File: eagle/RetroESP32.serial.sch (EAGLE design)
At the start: 70 parts, among them J1 AUDIO_JACK_3.5MM_KIT, J2 SPKR, J3 Batt Conn, J5 503182-1852_503182-1852, J6 USB4110-GF-A_REVB, Q3 DMG3415U-7, Q4 mmbt2222, Q5 mmbt2222, U1 ESP32-WROVER, U3 XC6210B332MR-G, U4 MCP73832T-2ACI/OT, U6 LM4875

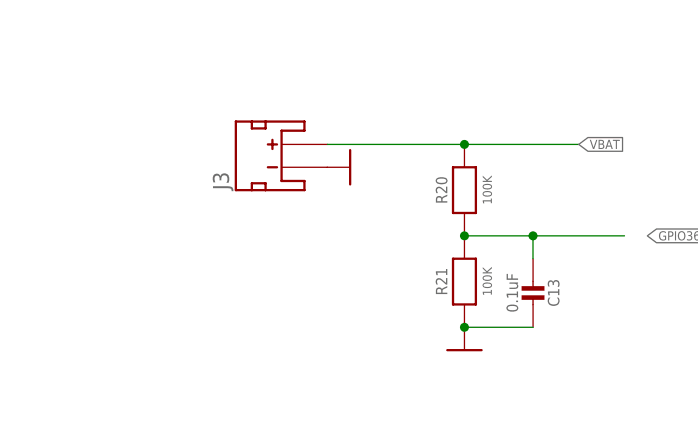
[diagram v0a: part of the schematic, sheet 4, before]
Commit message: feat: replaced JST with molex connector
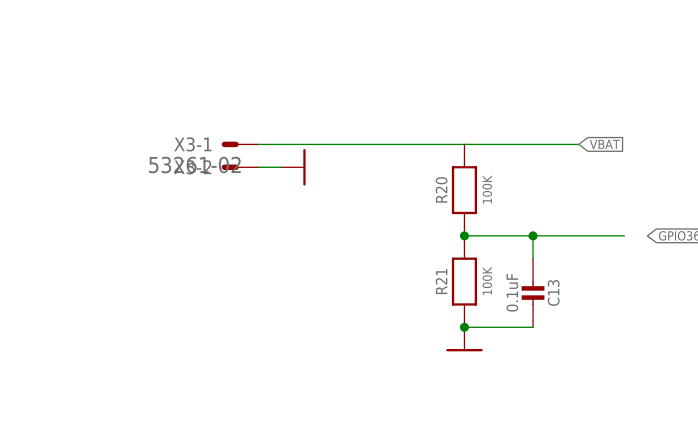
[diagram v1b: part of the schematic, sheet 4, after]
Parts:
- removed J2: SPKR, RetroESP32:CONN_02
- removed J3: Batt Conn, RetroESP32:JST_2MM_MALE
- added X2, X3: 53261-02, con-molex:53261-02
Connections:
- net GND: now also X3-2.S; no longer J3.-
- net VBAT: now also X3-1.S; no longer J3.+
- net VOUT1: now also X2-1.S; no longer J2.1
- net VOUT2: now also X2-2.S; no longer J2.2
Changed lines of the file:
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@@
 <layer number="56" name="wert" color="7" fill="1" visible="no" active="no"/>
 <layer number="57" name="tCAD" color="7" fill="1" visible="no" active="no"/>
+<layer number="58" name="b3D" color="7" fill="1" visible="no" active="no"/>
 <layer number="59" name="tCarbon" color="7" fill="1" visible="no" active="no"/>
 <layer number="60" name="bCarbon" color="7" fill="1" visible="no" active="no"/>
@@
 <layer number="154" name="FabDoc2" color="2" fill="1" visible="no" active="no"/>
 <layer number="155" name="FabDoc3" color="7" fill="15" visible="no" active="no"/>
+<layer number="156" name="DXF0409-TOP" color="7" fill="1" visible="no" active="no"/>
+<layer number="157" name="DXF0409-BOTTOM" color="7" fill="1" visible="no" active="no"/>
+<layer number="158" name="FaceMMeas" color="7" fill="1" visible="no" active="no"/>
+<layer number="159" name="Geh-Bear2" color="7" fill="1" visible="no" active="no"/>
+<layer number="160" name="Topologie" color="7" fill="1" visible="no" active="no"/>
+<layer number="161" name="tomplace2" color="7" fill="1" visible="no" active="no"/>
 <layer number="166" name="AntennaArea" color="7" fill="1" visible="yes" active="yes"/>
 <layer number="168" name="4mmHeightArea" color="7" fill="1" visible="yes" active="yes"/>
+<layer number="188" name="Graphics" color="15" fill="1" visible="yes" active="yes"/>
 <layer number="191" name="mNets" color="7" fill="1" visible="yes" active="yes"/>
 <layer number="192" name="mBusses" color="7" fill="1" visible="yes" active="yes"/>
@@
 <layer number="250" name="Descript" color="3" fill="1" visible="no" active="no"/>
 <layer number="251" name="SMDround" color="12" fill="11" visible="no" active="no"/>
+<layer number="252" name="BR-BS" color="7" fill="1" visible="no" active="no"/>
+<layer number="253" name="Extra" color="7" fill="1" visible="no" active="no"/>
 <layer number="254" name="cooling" color="7" fill="1" visible="yes" active="yes"/>
 <layer number="255" name="routoute" color="7" fill="1" visible="yes" active="yes"/>
@@
 <attribute name="MPN" value="ERJ-PA3J471V"/>
 </part>
-<part name="J3" library="RetroESP32" library_urn="urn:adsk.eagle:library:12566846" deviceset="JST_2MM_MALE" device="" package3d_urn="urn:adsk.eagle:package:12566919/2" override_package3d_urn="urn:adsk.eagle:package:12547802/2" override_package_urn="urn:adsk.eagle:footprint:12547803/1" override_locally_modified="yes" value="Batt Conn">
-<attribute name="MPN" value="S2B-PH-SM4-TB(LF)(SN)"/>
-</part>
-<part name="U$4" library="RetroESP32" library_urn="urn:adsk.eagle:library:12566846" deviceset="GND" device=""/>
 <part name="C6" library="RetroESP32" library_urn="urn:adsk.eagle:library:12566846" deviceset="CAP_CERAMIC" device="" package3d_urn="urn:adsk.eagle:package:12567032/2" override_package3d_urn="urn:adsk.eagle:package:12547722/2" override_package_urn="urn:adsk.eagle:footprint:12547723/1" override_locally_modified="yes" value="10uF">
 <attribute name="MPN" value="CL10A106MP8NNNC"/>
@@
 <attribute name="MPN" value="CL10A105KP8NNNC"/>
 </part>
-<part name="J2" library="RetroESP32" library_urn="urn:adsk.eagle:library:12566846" deviceset="CONN_02" device="" package3d_urn="urn:adsk.eagle:package:12566921/3" value="SPKR"/>
 <part name="C10" library="RetroESP32" library_urn="urn:adsk.eagle:library:12566846" deviceset="CAP_TANTALUM" device="A/3216_WAVE" package3d_urn="urn:adsk.eagle:package:12566925/3" override_package3d_urn="urn:adsk.eagle:package:12547719/2" override_package_urn="urn:adsk.eagle:footprint:12547720/1" override_locally_modified="yes" value="100uF">
 <attribute name="MPN" value="F930J107KAA"/>
@@
 <part name="R22" library="RetroESP32" library_urn="urn:adsk.eagle:library:12566846" deviceset="RESISTOR" device="0603MINI" package3d_urn="urn:adsk.eagle:package:12566926/2" override_package3d_urn="urn:adsk.eagle:package:12547690/2" override_package_urn="urn:adsk.eagle:footprint:12547691/1" override_locally_modified="yes" value="5.1K">
 <attribute name="MPN" value="ERJ-PA3F5101V"/>
+</part>
+<part name="X2" library="con-molex" library_urn="urn:adsk.eagle:library:165" deviceset="53?-02" device="261" package3d_urn="urn:adsk.eagle:package:8078537/1">
+<attribute name="MPN" value="0532614002"/>
+</part>
+<part name="U$2" library="RetroESP32" library_urn="urn:adsk.eagle:library:12566846" deviceset="GND" device=""/>
+<part name="X3" library="con-molex" library_urn="urn:adsk.eagle:library:165" deviceset="53?-02" device="261" package3d_urn="urn:adsk.eagle:package:8078537/1">
+<attribute name="MPN" value="0532614002"/>
 </part>
 </parts>
@@
 </plain>
 <instances>
-<instance part="J3" gate="G$1" x="33.02" y="106.68" smashed="yes" rot="R90">
-<attribute name="NAME" x="27.178" y="104.14" size="1.778" layer="95" rot="R90"/>
-<attribute name="MPN" x="33.02" y="106.68" size="1.778" layer="96" rot="R90" display="off"/>
-</instance>
-<instance part="U$4" gate="1" x="40.64" y="106.68" smashed="yes" rot="R90"/>
 <instance part="C6" gate="G$1" x="165.1" y="68.58" smashed="yes">
 <attribute name="NAME" x="162.81" y="69.83" size="1.27" layer="95" font="vector" rot="R90" align="center"/>
@@
 <attribute name="MPN" x="55.88" y="20.32" size="1.778" layer="96" rot="R90" display="off"/>
 </instance>
+<instance part="U$2" gate="1" x="35.56" y="106.68" smashed="yes" rot="R90"/>
+<instance part="X3" gate="-1" x="27.94" y="109.22" smashed="yes" rot="R180">
+<attribute name="NAME" x="25.4" y="109.982" size="1.524" layer="95" rot="R180"/>
+<attribute name="VALUE" x="28.702" y="107.823" size="1.778" layer="96" rot="R180"/>
+</instance>
+<instance part="X3" gate="-2" x="27.94" y="106.68" smashed="yes" rot="R180">
+<attribute name="NAME" x="25.4" y="107.442" size="1.524" layer="95" rot="R180"/>
+</instance>
 </instances>
 <busses>
@@
 <nets>
 <net name="GND" class="0">
-<segment>
-<pinref part="J3" gate="G$1" pin="-"/>
-<pinref part="U$4" gate="1" pin="GND"/>
-</segment>
 <segment>
 <pinref part="C6" gate="G$1" pin="1"/>
@@
 <pinref part="R22" gate="G$1" pin="1"/>
 </segment>
+<segment>
+<pinref part="U$2" gate="1" pin="GND"/>
+<wire x1="33.02" y1="106.68" x2="30.48" y2="106.68" width="0.1524" layer="91"/>
+<pinref part="X3" gate="-2" pin="S"/>
+</segment>
 </net>
 <net name="VBUS" class="0">
@@
 <net name="VBAT" class="0">
 <segment>
-<pinref part="J3" gate="G$1" pin="+"/>
-<wire x1="38.1" y1="109.22" x2="53.34" y2="109.22" width="0.1524" layer="91"/>
 <label x="66.04" y="109.22" size="1.016" layer="95" xref="yes"/>
 <pinref part="R20" gate="G$1" pin="2"/>
 <wire x1="53.34" y1="109.22" x2="66.04" y2="109.22" width="0.1524" layer="91"/>
-<junction x="53.34" y="109.22"/>
+<wire x1="53.34" y1="109.22" x2="30.48" y2="109.22" width="0.1524" layer="91"/>
+<pinref part="X3" gate="-1" pin="S"/>
 </segment>
 </net>
@@
 <attribute name="MPN" x="93.98" y="101.6" size="1.778" layer="96" rot="R90" display="off"/>
 </instance>
-<instance part="J2" gate="G$1" x="182.88" y="86.36" smashed="yes" rot="R180">
-<attribute name="VALUE" x="185.42" y="91.186" size="1.016" layer="96" font="vector" rot="R180"/>
-<attribute name="NAME" x="185.42" y="80.772" size="1.016" layer="95" font="vector" rot="R180"/>
-</instance>
 <instance part="C10" gate="G$1" x="144.78" y="114.3" smashed="yes" rot="R90">
 <attribute name="NAME" x="144.145" y="115.316" size="1.016" layer="95" font="vector" rot="R90"/>
@@
 <attribute name="NAME" x="21.59" y="92.329" size="1.016" layer="95"/>
 <attribute name="VALUE" x="21.59" y="90.17" size="1.016" layer="96"/>
+</instance>
+<instance part="X2" gate="-1" x="160.02" y="86.36" smashed="yes">
+<attribute name="NAME" x="162.56" y="85.598" size="1.524" layer="95"/>
+<attribute name="VALUE" x="159.258" y="87.757" size="1.778" layer="96"/>
+</instance>
+<instance part="X2" gate="-2" x="160.02" y="83.82" smashed="yes">
+<attribute name="NAME" x="162.56" y="83.058" size="1.524" layer="95"/>
 </instance>
 </instances>
@@
 <label x="139.7" y="114.3" size="1.016" layer="95" rot="MR0" xref="yes"/>
 <pinref part="C10" gate="G$1" pin="+"/>
+<junction x="139.7" y="114.3"/>
 </segment>
 <segment>
@@
 </segment>
 <segment>
-<pinref part="J2" gate="G$1" pin="1"/>
-<wire x1="175.26" y1="86.36" x2="172.72" y2="86.36" width="0.1524" layer="91"/>
-<label x="172.72" y="86.36" size="1.016" layer="95" rot="MR0" xref="yes"/>
+<wire x1="157.48" y1="86.36" x2="152.4" y2="86.36" width="0.1524" layer="91"/>
+<label x="152.4" y="86.36" size="1.016" layer="95" rot="R180" xref="yes"/>
+<pinref part="X2" gate="-1" pin="S"/>
 </segment>
 </net>
@@
 </segment>
 <segment>
-<pinref part="J2" gate="G$1" pin="2"/>
-<wire x1="175.26" y1="83.82" x2="172.72" y2="83.82" width="0.1524" layer="91"/>
-<label x="172.72" y="83.82" size="1.016" layer="95" rot="MR0" xref="yes"/>
-</segment>
-</net>
+<wire x1="157.48" y1="83.82" x2="152.4" y2="83.82" width="0.1524" layer="91"/>
+<label x="152.4" y="83.82" size="1.016" layer="95" rot="R180" xref="yes"/>
+<pinref part="X2" gate="-2" pin="S"/>
+</segment>
+</net>

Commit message: feat: released X
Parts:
- added D1: LTST-C155GEKT, LTST-C155GEKT:LTST-C155GEKT
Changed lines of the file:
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@@
 <attribute name="MPN" value="0532614002"/>
 </part>
+<part name="D1" library="LTST-C155GEKT" deviceset="LTST-C155GEKT" device=""/>
 </parts>
 <sheets>
@@
 <attribute name="MPN" x="132.08" y="53.34" size="1.778" layer="96" display="off"/>
 </instance>
+<instance part="D1" gate="G$1" x="114.3" y="43.18" smashed="yes">
+<attribute name="NAME" x="111.2012" y="47.6758" size="1.27" layer="95"/>
+<attribute name="VALUE" x="110.744" y="39.878" size="1.27" layer="96"/>
+</instance>
+<instance part="D1" gate="G$2" x="114.3" y="38.1" smashed="yes">
+<attribute name="NAME" x="111.2012" y="42.5958" size="1.27" layer="95"/>
+<attribute name="VALUE" x="110.744" y="34.798" size="1.27" layer="96"/>
+</instance>
 </instances>

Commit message: update: BOM for X
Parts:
- removed D1: LTST-C155GEKT, LTST-C155GEKT:LTST-C155GEKT
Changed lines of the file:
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@@
 <attribute name="MPN" value="0532614002"/>
 </part>
-<part name="D1" library="LTST-C155GEKT" deviceset="LTST-C155GEKT" device=""/>
 </parts>
 <sheets>
@@
 <attribute name="MPN" x="132.08" y="53.34" size="1.778" layer="96" display="off"/>
 </instance>
-<instance part="D1" gate="G$1" x="114.3" y="43.18" smashed="yes">
-<attribute name="NAME" x="111.2012" y="47.6758" size="1.27" layer="95"/>
-<attribute name="VALUE" x="110.744" y="39.878" size="1.27" layer="96"/>
-</instance>
-<instance part="D1" gate="G$2" x="114.3" y="38.1" smashed="yes">
-<attribute name="NAME" x="111.2012" y="42.5958" size="1.27" layer="95"/>
-<attribute name="VALUE" x="110.744" y="34.798" size="1.27" layer="96"/>
-</instance>
 </instances>
